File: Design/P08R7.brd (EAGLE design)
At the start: 28 x 26.6 mm, 26 parts, among them P1 PENTABIT_17.32, U1 STM32G0B1CEU6N, U2 VL53L1CXV0FY_1, X1 XTALL_CSTCE8M00G52

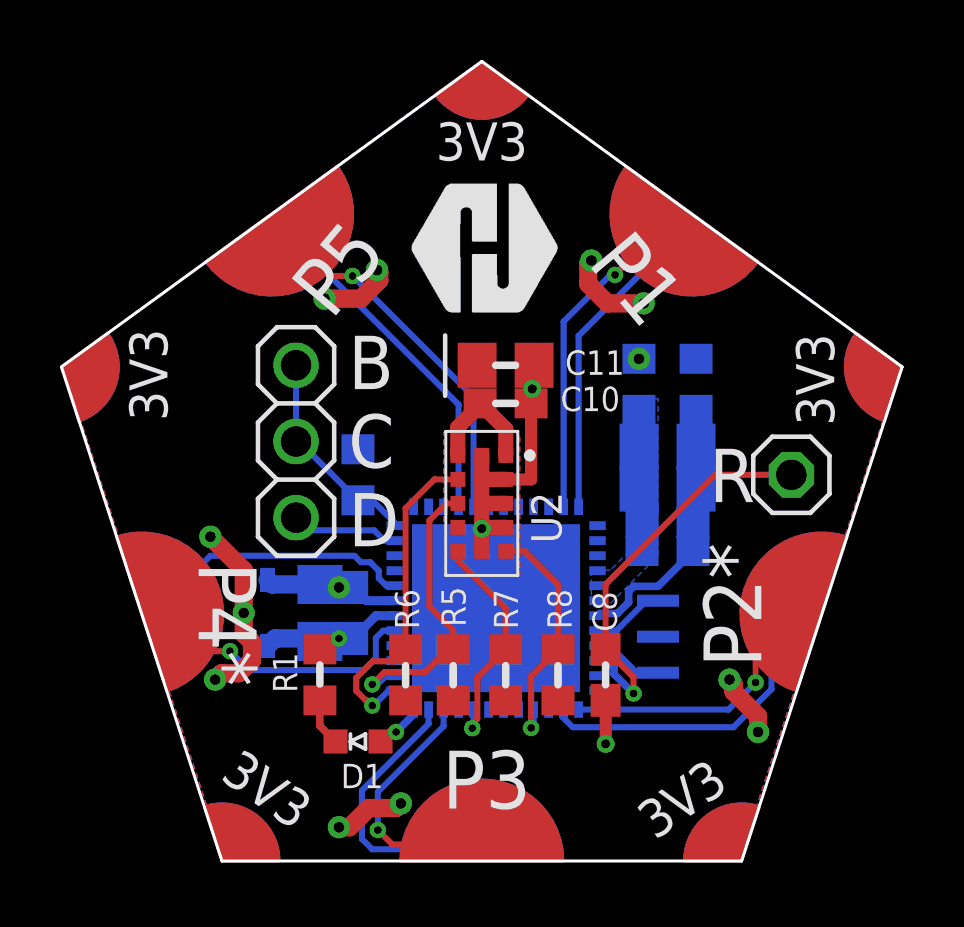
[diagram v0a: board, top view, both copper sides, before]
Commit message: -Add TVS diode -Change the MCU to STM32G0B1CEU6 -Activate the thermal option for the polygon
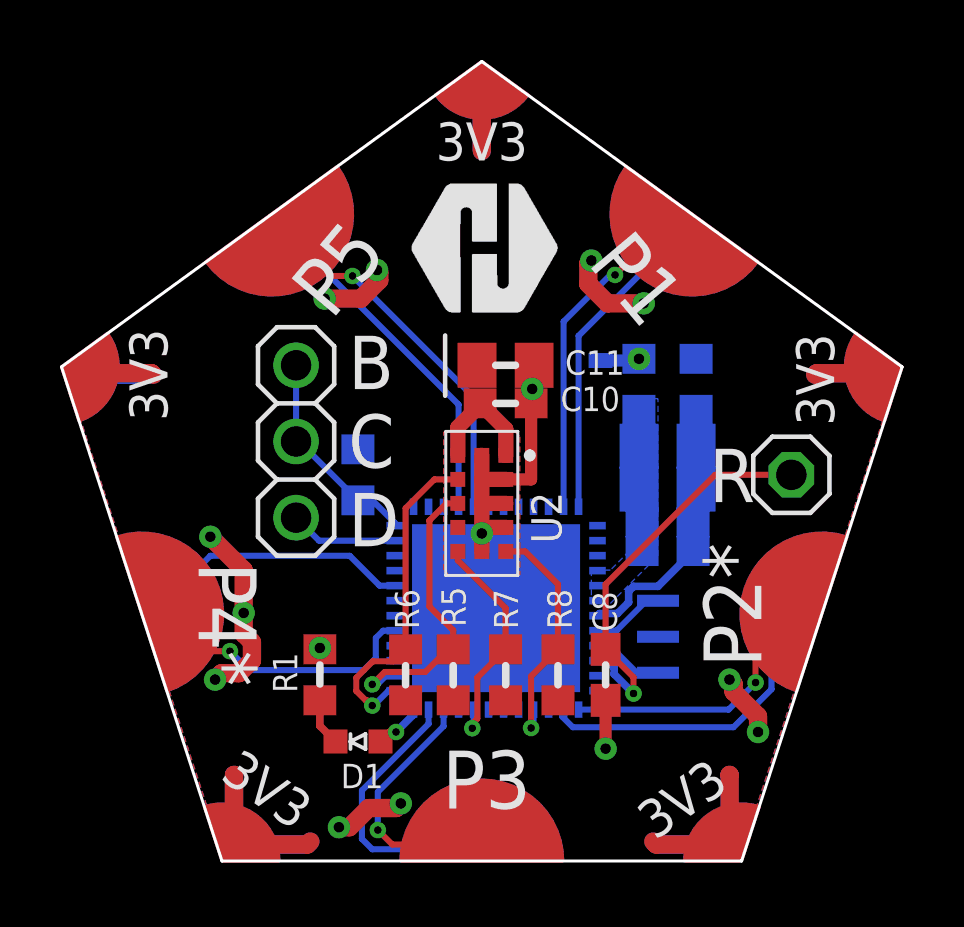
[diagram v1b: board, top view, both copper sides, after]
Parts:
- removed C3: 100nF, HEXABITZ_RCLS:C-0603
- removed C4: 4.7uF, HEXABITZ_RCLS:C-0805-POL
- U1: value STM32G0B1CEU6N -> STM32G0B1CEU6QFN_B1CEU6_STM-L; device HEXABITZ_ICs:HEXABITZ_ICS_QFN_B1CEU6_STM-L -> HEXABITZ_ICs:QFN_B1CEU6_STM-L
- moved D2 13.1 mm to (2.86, 4.76), turned to 180 degrees
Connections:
- net GND: no longer C3.2, C4.2, U1.30
- net VDD: no longer C3.1, C4.1, U1.31
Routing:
- net GND: track 33.5 -> 48.1 mm
- net VDD: track 8.66 -> 22.3 mm, vias 2 -> 1
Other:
- board text added: "P08R70"
- board text removed: "H08R70"
